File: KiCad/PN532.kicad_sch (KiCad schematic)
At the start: 55 parts, among them J1 Bell, J2 SPOX, SW1 TAMPER, U1 PN532, U2 QR, U3 QR, Y1 27.12MHz

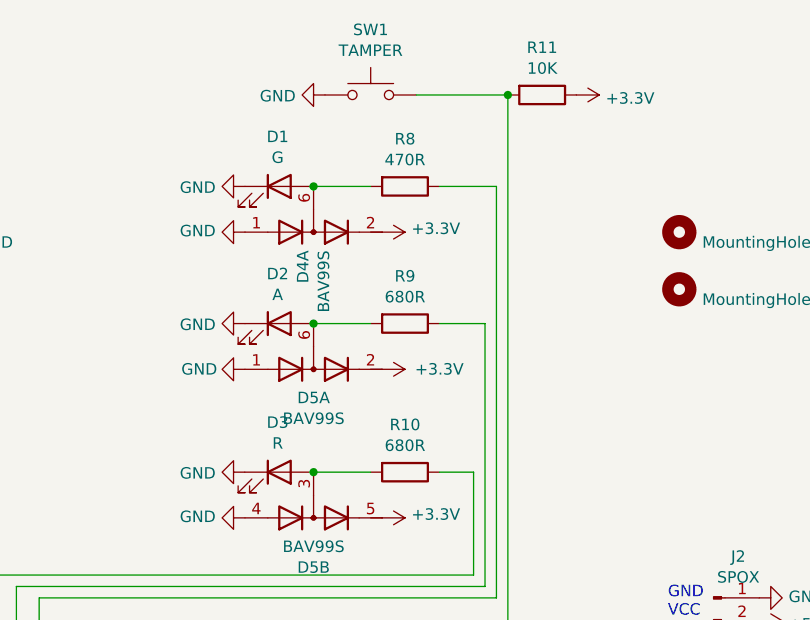
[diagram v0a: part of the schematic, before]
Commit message: Reverse mount LEDs
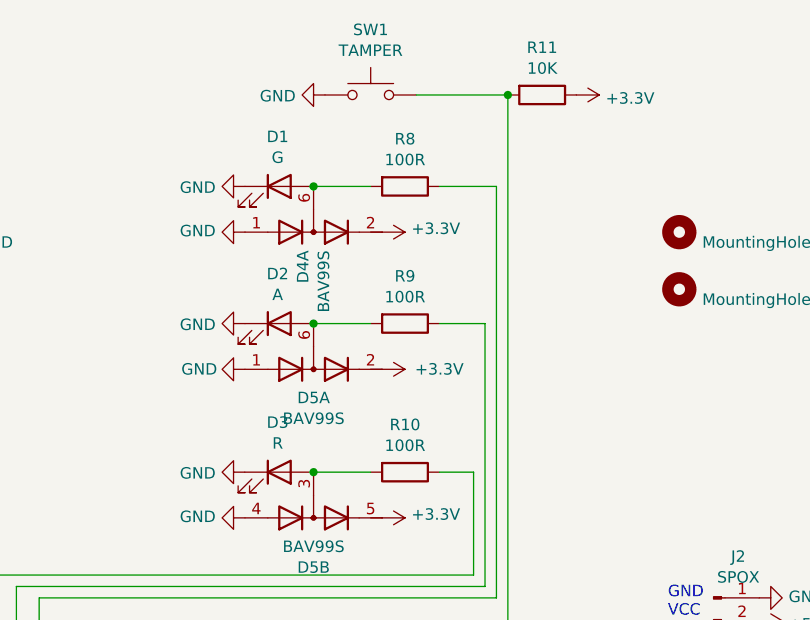
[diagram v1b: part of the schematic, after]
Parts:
- D1: footprint RevK:LED_Reverse -> RevK:STP_156120xx7530; Manufacturer Kingbright -> Wurth Elektronik; Note 0603 mounted face down -> Reverse mount LED; Part No APTD1608LCGCK -> 156120VS75300
- D2: footprint RevK:LED_Reverse -> RevK:STP_156120xx7530; Manufacturer Kingbright -> Wurth Elektronik; Note 0603 mounted face down -> Reverse mount LED; Part No APHD1608LSYCK -> 156120YS75300
- D3: footprint RevK:LED_Reverse -> RevK:STP_156120xx7530; Manufacturer Kingbright -> Wurth Elektronik; Note 0603 mounted face down -> Reverse mount LED; Part No APHD1608LSURCK -> 156120RS75300
- R10, R9: value 680R -> 100R; Part No RC0603JR-07680RL -> RC0603JR-07100RL
- R8: value 470R -> 100R; Part No AC0603JR-07470RL -> RC0603JR-07100RL
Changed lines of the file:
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@@
     (property "Reference" "D1" (id 0) (at 199.2122 24.9682 0))
     (property "Value" "G" (id 1) (at 199.2122 27.2796 0))
-    (property "Footprint" "RevK:LED_Reverse" (id 2) (at 199.39 30.48 0)
-      (effects (font (size 1.27 1.27)) hide)
-    )
-    (property "Datasheet" "https://www.mouser.co.uk/ProductDetail/604-APTD1608LCGCK" (id 3) (at 199.39 30.48 0)
-      (effects (font (size 1.27 1.27)) hide)
-    )
-    (property "Note" "0603 mounted face down" (id 4) (at 199.39 30.48 0)
-      (effects (font (size 1.27 1.27)) hide)
-    )
-    (property "Part No" "APTD1608LCGCK" (id 5) (at 199.39 30.48 0)
-      (effects (font (size 1.27 1.27)) hide)
-    )
-    (property "Manufacturer" "Kingbright" (id 6) (at 199.39 30.48 0)
+    (property "Footprint" "RevK:STP_156120xx7530" (id 2) (at 199.39 30.48 0)
+      (effects (font (size 1.27 1.27)) hide)
+    )
+    (property "Datasheet" "https://www.mouser.co.uk/ProductDetail/710-156120VS75300" (id 3) (at 199.39 30.48 0)
+      (effects (font (size 1.27 1.27)) hide)
+    )
+    (property "Note" "Reverse mount LED" (id 4) (at 199.39 30.48 0)
+      (effects (font (size 1.27 1.27)) hide)
+    )
+    (property "Part No" "156120VS75300" (id 5) (at 199.39 30.48 0)
+      (effects (font (size 1.27 1.27)) hide)
+    )
+    (property "Manufacturer" "Wurth Elektronik" (id 6) (at 199.39 30.48 0)
       (effects (font (size 1.27 1.27)) hide)
     )
@@
     (property "Reference" "D2" (id 0) (at 199.2122 40.2082 0))
     (property "Value" "A" (id 1) (at 199.2122 42.5196 0))
-    (property "Footprint" "RevK:LED_Reverse" (id 2) (at 199.39 45.72 0)
-      (effects (font (size 1.27 1.27)) hide)
-    )
-    (property "Datasheet" "https://www.mouser.co.uk/ProductDetail/604-APHD1608LSYCK" (id 3) (at 199.39 45.72 0)
-      (effects (font (size 1.27 1.27)) hide)
-    )
-    (property "Note" "0603 mounted face down" (id 4) (at 199.39 45.72 0)
-      (effects (font (size 1.27 1.27)) hide)
-    )
-    (property "Part No" "APHD1608LSYCK" (id 5) (at 199.39 45.72 0)
-      (effects (font (size 1.27 1.27)) hide)
-    )
-    (property "Manufacturer" "Kingbright" (id 6) (at 199.39 45.72 0)
+    (property "Footprint" "RevK:STP_156120xx7530" (id 2) (at 199.39 45.72 0)
+      (effects (font (size 1.27 1.27)) hide)
+    )
+    (property "Datasheet" "https://www.mouser.co.uk/ProductDetail/710-156120YS75300" (id 3) (at 199.39 45.72 0)
+      (effects (font (size 1.27 1.27)) hide)
+    )
+    (property "Note" "Reverse mount LED" (id 4) (at 199.39 45.72 0)
+      (effects (font (size 1.27 1.27)) hide)
+    )
+    (property "Part No" "156120YS75300" (id 5) (at 199.39 45.72 0)
+      (effects (font (size 1.27 1.27)) hide)
+    )
+    (property "Manufacturer" "Wurth Elektronik" (id 6) (at 199.39 45.72 0)
       (effects (font (size 1.27 1.27)) hide)
     )
@@
     (property "Reference" "D3" (id 0) (at 199.2122 56.7182 0))
     (property "Value" "R" (id 1) (at 199.2122 59.0296 0))
-    (property "Footprint" "RevK:LED_Reverse" (id 2) (at 199.39 62.23 0)
-      (effects (font (size 1.27 1.27)) hide)
-    )
-    (property "Datasheet" "https://www.mouser.co.uk/ProductDetail/604-APHD1608LSURCK" (id 3) (at 199.39 62.23 0)
-      (effects (font (size 1.27 1.27)) hide)
-    )
-    (property "Note" "0603 mounted face down" (id 4) (at 199.39 62.23 0)
-      (effects (font (size 1.27 1.27)) hide)
-    )
-    (property "Part No" "APHD1608LSURCK" (id 5) (at 199.39 62.23 0)
-      (effects (font (size 1.27 1.27)) hide)
-    )
-    (property "Manufacturer" "Kingbright" (id 6) (at 199.39 62.23 0)
+    (property "Footprint" "RevK:STP_156120xx7530" (id 2) (at 199.39 62.23 0)
+      (effects (font (size 1.27 1.27)) hide)
+    )
+    (property "Datasheet" "https://www.mouser.co.uk/ProductDetail/710-156120RS75300" (id 3) (at 199.39 62.23 0)
+      (effects (font (size 1.27 1.27)) hide)
+    )
+    (property "Note" "Reverse mount LED" (id 4) (at 199.39 62.23 0)
+      (effects (font (size 1.27 1.27)) hide)
+    )
+    (property "Part No" "156120RS75300" (id 5) (at 199.39 62.23 0)
+      (effects (font (size 1.27 1.27)) hide)
+    )
+    (property "Manufacturer" "Wurth Elektronik" (id 6) (at 199.39 62.23 0)
       (effects (font (size 1.27 1.27)) hide)
     )
@@
     (in_bom yes) (on_board yes)
     (property "Reference" "R8" (id 0) (at 213.36 25.2222 90))
-    (property "Value" "470R" (id 1) (at 213.36 27.5336 90))
+    (property "Value" "100R" (id 1) (at 213.36 27.5336 90))
     (property "Footprint" "RevK:R_0603" (id 2) (at 213.36 28.702 90)
       (effects (font (size 1.27 1.27)) hide)
     )
-    (property "Datasheet" "https://www.mouser.co.uk/ProductDetail/603-AC0603JR-07470RL" (id 3) (at 213.36 30.48 0)
+    (property "Datasheet" "https://www.mouser.co.uk/ProductDetail/603-RC0603JR-07100RL" (id 3) (at 213.36 30.48 0)
       (effects (font (size 1.27 1.27)) hide)
     )
@@
       (effects (font (size 1.27 1.27)) hide)
     )
-    (property "Part No" "AC0603JR-07470RL" (id 5) (at 213.36 30.48 90)
+    (property "Part No" "RC0603JR-07100RL" (id 5) (at 213.36 30.48 90)
       (effects (font (size 1.27 1.27)) hide)
     )
@@
     (in_bom yes) (on_board yes)
     (property "Reference" "R9" (id 0) (at 213.36 40.4622 90))
-    (property "Value" "680R" (id 1) (at 213.36 42.7736 90))
+    (property "Value" "100R" (id 1) (at 213.36 42.7736 90))
     (property "Footprint" "RevK:R_0603" (id 2) (at 213.36 43.942 90)
       (effects (font (size 1.27 1.27)) hide)
     )
-    (property "Datasheet" "https://www.mouser.co.uk/ProductDetail/603-RC0603JR-07680RL" (id 3) (at 213.36 45.72 0)
+    (property "Datasheet" "https://www.mouser.co.uk/ProductDetail/603-RC0603JR-07100RL" (id 3) (at 213.36 45.72 0)
       (effects (font (size 1.27 1.27)) hide)
     )
@@
       (effects (font (size 1.27 1.27)) hide)
     )
-    (property "Part No" "RC0603JR-07680RL" (id 5) (at 213.36 45.72 90)
+    (property "Part No" "RC0603JR-07100RL" (id 5) (at 213.36 45.72 90)
       (effects (font (size 1.27 1.27)) hide)
     )
@@
     (in_bom yes) (on_board yes)
     (property "Reference" "R10" (id 0) (at 213.36 56.9722 90))
-    (property "Value" "680R" (id 1) (at 213.36 59.2836 90))
+    (property "Value" "100R" (id 1) (at 213.36 59.2836 90))
     (property "Footprint" "RevK:R_0603" (id 2) (at 213.36 60.452 90)
       (effects (font (size 1.27 1.27)) hide)
     )
-    (property "Datasheet" "https://www.mouser.co.uk/ProductDetail/603-RC0603JR-07680RL" (id 3) (at 213.36 62.23 0)
+    (property "Datasheet" "https://www.mouser.co.uk/ProductDetail/603-RC0603JR-07100RL" (id 3) (at 213.36 62.23 0)
       (effects (font (size 1.27 1.27)) hide)
     )
@@
       (effects (font (size 1.27 1.27)) hide)
     )
-    (property "Part No" "RC0603JR-07680RL" (id 5) (at 213.36 62.23 90)
+    (property "Part No" "RC0603JR-07100RL" (id 5) (at 213.36 62.23 90)
       (effects (font (size 1.27 1.27)) hide)
     )
@@
     )
     (path "/00000000-0000-0000-0000-0000607e9287"
-      (reference "D1") (unit 1) (value "G") (footprint "RevK:LED_Reverse")
+      (reference "D1") (unit 1) (value "G") (footprint "RevK:STP_156120xx7530")
     )
     (path "/00000000-0000-0000-0000-0000607eaf87"
-      (reference "D2") (unit 1) (value "A") (footprint "RevK:LED_Reverse")
+      (reference "D2") (unit 1) (value "A") (footprint "RevK:STP_156120xx7530")
     )
     (path "/00000000-0000-0000-0000-0000607eb52d"
-      (reference "D3") (unit 1) (value "R") (footprint "RevK:LED_Reverse")
+      (reference "D3") (unit 1) (value "R") (footprint "RevK:STP_156120xx7530")
     )
     (path "/00000000-0000-0000-0000-0000609ca448"
@@
     )
     (path "/00000000-0000-0000-0000-0000607ebc51"
-      (reference "R8") (unit 1) (value "470R") (footprint "RevK:R_0603")
+      (reference "R8") (unit 1) (value "100R") (footprint "RevK:R_0603")
     )
     (path "/00000000-0000-0000-0000-0000607ed1a6"
-      (reference "R9") (unit 1) (value "680R") (footprint "RevK:R_0603")
+      (reference "R9") (unit 1) (value "100R") (footprint "RevK:R_0603")
     )
     (path "/00000000-0000-0000-0000-0000607ed794"
-      (reference "R10") (unit 1) (value "680R") (footprint "RevK:R_0603")
+      (reference "R10") (unit 1) (value "100R") (footprint "RevK:R_0603")
     )
     (path "/00000000-0000-0000-0000-00006080249e"

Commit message: Cleanup BOM more
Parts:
- C10, C13, C15: Manufacturer Samsung Electro-Mechanics -> (none); Note 0603 -> (none); Part No CL10A475KP8NNNC -> 0603-4.7uF-10V
- C11, C12, C18, C7, C9: Manufacturer KEMET -> (none); Note 0603 -> (none); Part No C0603C104M4RACTU -> 0603-100nF-25V
- C14: Note 0603 -> (none); Part No (none) -> 0603-100nF-25V
- C16, C17: Manufacturer Walsin -> (none); Note 0603 -> (none); Part No 0603N220F500CT -> 0603-22pF-50V
- C19: Manufacturer KEMET -> (none); Note 0603 -> (none); Part No C0603C330G8HACTU -> 0603-33pF-50V
- C5, C6: Manufacturer Vishay / Vitramon -> (none); Note 0603 -> (none); Part No VJ0603A221GXAPW1BC -> 0603-220pF-50V
- R1, R3: Manufacturer Bourns -> (none); Note 0603 -> (none); Part No CR0603-J/-000ELF -> 0603-0R
- R10: Manufacturer YAGE -> (none); Note 0603 -> (none); Part No RC0603JR-07100RL -> 0603-100R
- R11, R15, R6: Manufacturer Bourns -> (none); Note 0603 -> (none); Part No CR0603-FX-1002ELF -> 0603-10K
- R12, R13, R14, R8, R9: Manufacturer YAGEO -> (none); Note 0603 -> (none); Part No RC0603JR-07100RL -> 0603-100R
- R2: Manufacturer YAGEO -> (none); Note 0805 -> (none); Part No RC0603FR-102K7L -> 0805-0R

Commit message: As ordered from PCB Train today
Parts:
- Y1: Manufacturer Wurth Elektronik -> ABRACON; Part No 830053099 -> ABM81-27.120MHZ-10-B1U-T3
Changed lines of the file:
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@@
       (effects (font (size 1.27 1.27)) hide)
     )
-    (property "Datasheet" "https://www.mouser.co.uk/ProductDetail/710-830053099" (id 3) (at 158.75 144.78 0)
+    (property "Datasheet" "https://www.mouser.co.uk/ProductDetail/815-ABM81-271-10B1UT" (id 3) (at 158.75 144.78 0)
       (effects (font (size 1.27 1.27)) hide)
     )
-    (property "Part No" "830053099" (id 4) (at 158.75 144.78 0)
+    (property "Part No" "ABM81-27.120MHZ-10-B1U-T3" (id 4) (at 158.75 144.78 0)
       (effects (font (size 1.27 1.27)) hide)
     )
-    (property "Manufacturer" "Wurth Elektronik" (id 5) (at 158.75 144.78 0)
+    (property "Manufacturer" "ABRACON" (id 5) (at 158.75 144.78 0)
       (effects (font (size 1.27 1.27)) hide)
     )

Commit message: Minor tweaks, all looking good.
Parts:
- JP1: footprint Jumper:SolderJumper-3_P1.3mm_Bridged2Bar12_RoundedPad1.0x1.5mm_NumberLabels -> RevK:SolderJumper3
- SW1: now left out of the parts list
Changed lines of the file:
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@@
   )
   (symbol (lib_id "Switch:SW_Push") (at 209.55 20.32 0) (unit 1)
-    (in_bom yes) (on_board yes)
+    (in_bom no) (on_board yes)
     (property "Reference" "SW1" (id 0) (at 209.55 13.081 0))
     (property "Value" "TAMPER" (id 1) (at 209.55 15.3924 0))
@@
       (effects (font (size 1.27 1.27)) (justify left))
     )
-    (property "Footprint" "Jumper:SolderJumper-3_P1.3mm_Bridged2Bar12_RoundedPad1.0x1.5mm_NumberLabels" (id 2) (at 193.04 148.59 0)
+    (property "Footprint" "RevK:SolderJumper3" (id 2) (at 193.04 148.59 0)
       (effects (font (size 1.27 1.27)) hide)
     )
@@
     )
     (path "/00000000-0000-0000-0000-0000609405db"
-      (reference "JP1") (unit 1) (value "I1") (footprint "Jumper:SolderJumper-3_P1.3mm_Bridged2Bar12_RoundedPad1.0x1.5mm_NumberLabels")
+      (reference "JP1") (unit 1) (value "I1") (footprint "RevK:SolderJumper3")
     )
     (path "/00000000-0000-0000-0000-00006075bc21"
